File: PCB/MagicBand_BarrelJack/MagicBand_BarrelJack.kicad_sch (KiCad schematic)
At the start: 19 parts, among them J2 MFRC522_Module, J3 RF_TX_DFLIFE, J6 NeoPixel_LED_Strip, J8 PWR_IN_BarrelJack_BareLeads, J9 ISP_AVR_2x3, Q1 AO3401A_PMOS_G-S-D, U1 ATmega328P-P, U2 MCP1700-3302, Y1 16MHz

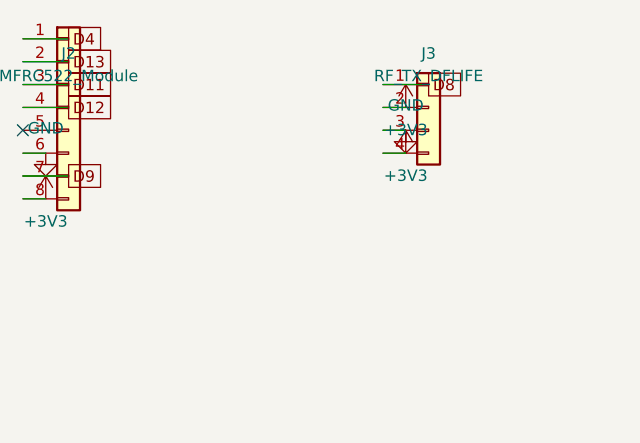
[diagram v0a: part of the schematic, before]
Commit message: Correct J3 pin 4: leave no-connect, don't wire to +3V3
Prior commit wired the Enable pin to +3V3, reading the module's
"connected to power supply, no function" listing text as an external
wiring requirement. User clarified: that describes the module's
internal wiring, not an instruction for us -- it's a dead pin that
just needs a physical pad to seat into, not a net. Reverts the
schematic wire/power-symbol and the PCB pad's net assignment; the
1x03->1x04 footprint swap itself stands, that part was never in
question. ERC back to exact baseline (129), DRC unchanged (16
violations, 0 unconnected instead of 1, since there's nothing to
route to pad 4 now).

Co-Authored-By: Claude Sonnet 5 <noreply@anthropic.com>
Claude-Session: https://claude.ai/code/session_01UiULxbNnG293uuE4csn9nG
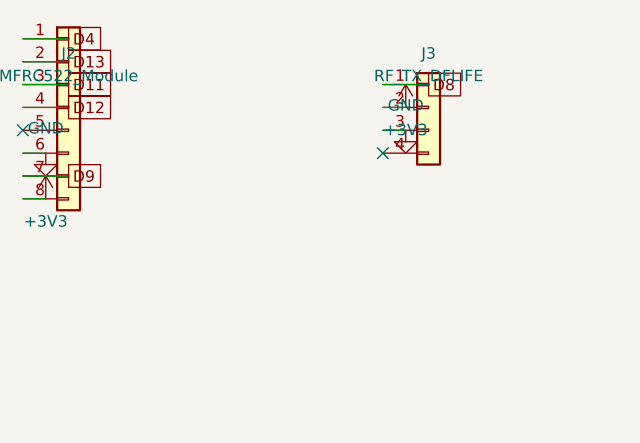
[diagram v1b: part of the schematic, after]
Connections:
- net +3V3: no longer J3.4 (Pin_4)
- no-connect marks 13 -> 14
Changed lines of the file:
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@@
 		)
 	)
-	(wire
-		(pts (xy 284.92 45.08) (xy 287.46 45.08))
-		(stroke (width 0) (type default))
-	)
+	(no_connect (at 284.92 45.08))
 	(wire
 		(pts (xy 284.92 37.46) (xy 290.0 37.46))
@@
 					(unit 1)
 				)
-			)
-		)
-	)
-	(symbol
-		(lib_id "power:+3V3")
-		(at 287.46 45.08 0)
-		(unit 1)
-		(exclude_from_sim no)
-		(in_bom yes)
-		(on_board yes)
-		(dnp no)
-		(property "Reference" "#PWRf03f"
-			(at 287.46 41.58 0)
-			(effects (font (size 1.27 1.27)) (hide yes))
-		)
-		(property "Value" "+3V3"
-			(at 287.46 47.58 0)
-			(effects (font (size 1.27 1.27)))
-		)
-		(property "Footprint" ""
-			(at 287.46 45.08 0)
-			(effects (font (size 1.27 1.27)) (hide yes))
-		)
-		(property "Datasheet" ""
-			(at 287.46 45.08 0)
-			(effects (font (size 1.27 1.27)) (hide yes))
-		)
-		(pin "1")
-		(instances
-			(project "MagicBand_BarrelJack"
-				(path "/bcfef247-dfd6-4ae3-b42f-2bc22ccfcf8a"
-					(reference "#PWRf03f")
-					(unit 1)
-				)

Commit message: Wire J3 Enable pin to +3V3, swap footprint 1x03 -> 1x04
Resolves the 2026-08-14 open decision (skip the pad vs. wire it up) in
favor of wiring it: the D-FLIFE TX module's Enable pin must be tied to
power per its documented pinout, it isn't a usable control pin. Adds
pin 4 to J3's schematic symbol and PCB footprint; GUI reroute (zone
refill, pad 4 routing, J3/J6 courtyard nudge) still needed before this
is fab-ready, tracked in Work Packages.

Co-Authored-By: Claude Sonnet 5 <noreply@anthropic.com>
Claude-Session: https://claude.ai/code/session_01UiULxbNnG293uuE4csn9nG
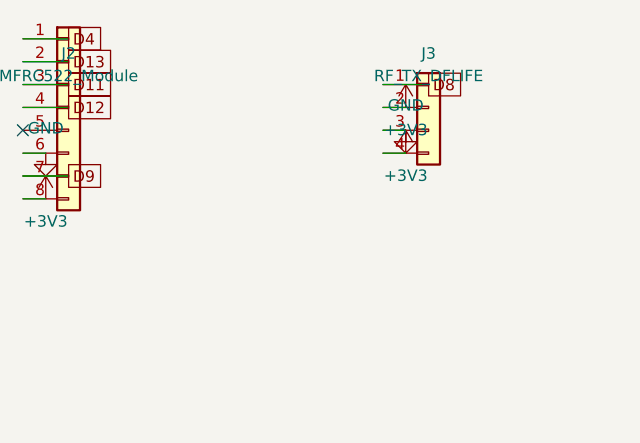
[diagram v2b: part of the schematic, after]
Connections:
- net +3V3: now also J3.4 (Pin_4)
- no-connect marks 14 -> 13
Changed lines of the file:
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@@
 		)
 	)
-	(no_connect (at 284.92 45.08))
+	(wire
+		(pts (xy 284.92 45.08) (xy 287.46 45.08))
+		(stroke (width 0) (type default))
+	)
 	(wire
 		(pts (xy 284.92 37.46) (xy 290.0 37.46))
@@
 					(unit 1)
 				)
+			)
+		)
+	)
+	(symbol
+		(lib_id "power:+3V3")
+		(at 287.46 45.08 0)
+		(unit 1)
+		(exclude_from_sim no)
+		(in_bom yes)
+		(on_board yes)
+		(dnp no)
+		(property "Reference" "#PWRf03f"
+			(at 287.46 41.58 0)
+			(effects (font (size 1.27 1.27)) (hide yes))
+		)
+		(property "Value" "+3V3"
+			(at 287.46 47.58 0)
+			(effects (font (size 1.27 1.27)))
+		)
+		(property "Footprint" ""
+			(at 287.46 45.08 0)
+			(effects (font (size 1.27 1.27)) (hide yes))
+		)
+		(property "Datasheet" ""
+			(at 287.46 45.08 0)
+			(effects (font (size 1.27 1.27)) (hide yes))
+		)
+		(pin "1")
+		(instances
+			(project "MagicBand_BarrelJack"
+				(path "/bcfef247-dfd6-4ae3-b42f-2bc22ccfcf8a"
+					(reference "#PWRf03f")
+					(unit 1)
+				)
